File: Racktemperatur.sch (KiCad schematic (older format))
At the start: 16 parts, among them J1 Conn_01x03, J2 Conn_01x03, J3 Barrel_Jack_MountingPin, Q1 IRLZ44N, U1 74HC595, U2 74HC595, U3 DS18B20

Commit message: Version 1.3 as rack mount
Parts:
- added J4: Screw_Terminal_01x02, TerminalBlock:TerminalBlock_bornier-2_P5.08mm, symbol Connector:Screw_Terminal_01x02
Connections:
- net GND: now also J4.1 (Pin_1)
- net at A1.16 (D13): now also J4.2 (Pin_2)
- no-connect marks 22 -> 25
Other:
- moved on the sheet: R1, R2
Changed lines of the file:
@@
 EESchema Schematic File Version 4
 LIBS:Racktemperatur-cache
-EELAYER 29 0
+EELAYER 30 0
 EELAYER END
 $Descr A4 11693 8268
@@
 Sheet 1 1
 Title "Rack Temperature Control"
-Date "2019-06-03"
-Rev "1.2"
+Date "2019-10-25"
+Rev "1.3"
 Comp "haus-automatisierung.com"
 Comment1 "Matthias Kleine"
@@
 U 1 1 5CA724F1
 P 3800 5300
-F 0 "U1" H 3800 6078 50  0000 C CNN
-F 1 "74HC595" H 3800 5987 50  0000 C CNN
+F 0 "U1" H 3550 5850 50  0000 C CNN
+F 1 "74HC595" H 4000 5850 50  0000 C CNN
 F 2 "Package_DIP:DIP-16_W7.62mm_LongPads" H 3800 5300 50  0001 C CNN
 F 3 "http://www.ti.com/lit/ds/symlink/sn74hc595.pdf" H 3800 5300 50  0001 C CNN
@@
 U 1 1 5CA72541
 P 6450 5250
-F 0 "U2" H 6450 6028 50  0000 C CNN
-F 1 "74HC595" H 6450 5937 50  0000 C CNN
+F 0 "U2" H 6200 5800 50  0000 C CNN
+F 1 "74HC595" H 6650 5800 50  0000 C CNN
 F 2 "Package_DIP:DIP-16_W7.62mm_LongPads" H 6450 5250 50  0001 C CNN
 F 3 "http://www.ti.com/lit/ds/symlink/sn74hc595.pdf" H 6450 5250 50  0001 C CNN
@@
 U 1 1 5CA72A4D
 P 5650 3100
-F 0 "A1" H 5650 2014 50  0000 C CNN
-F 1 "Arduino_Nano_v3.x" H 5650 1923 50  0000 C CNN
+F 0 "A1" H 6000 4050 50  0000 C CNN
+F 1 "Arduino_Nano_v3.x" H 5050 4050 50  0000 C CNN
 F 2 "Module:Arduino_Nano_WithMountingHoles" H 5800 2150 50  0001 L CNN
 F 3 "http://www.mouser.com/pdfdocs/Gravitech_Arduino_Nano3_0.pdf" H 5650 2100 50  0001 C CNN
@@
 Connection ~ 5650 6250
 Wire Wire Line
-	5650 4100 5650 5450
+	5650 4100 5650 4250
 Wire Wire Line
 	5750 2100 5750 1950
@@
 L Device:R R1
 U 1 1 5CA7E658
-P 5400 6100
-F 0 "R1" H 5470 6146 50  0000 L CNN
-F 1 "100Ω" H 5470 6055 50  0000 L CNN
-F 2 "Resistor_SMD:R_0805_2012Metric_Pad1.15x1.40mm_HandSolder" V 5330 6100 50  0001 C CNN
-F 3 "~" H 5400 6100 50  0001 C CNN
-	1    5400 6100
+P 5500 6100
+F 0 "R1" H 5570 6146 50  0000 L CNN
+F 1 "100Ω" H 5570 6055 50  0000 L CNN
+F 2 "Resistor_SMD:R_0805_2012Metric_Pad1.15x1.40mm_HandSolder" V 5430 6100 50  0001 C CNN
+F 3 "~" H 5500 6100 50  0001 C CNN
+	1    5500 6100
 	1    0    0    -1
 $EndComp
@@
 L Device:R R2
 U 1 1 5CA7E6C1
-P 8050 6100
-F 0 "R2" H 8120 6146 50  0000 L CNN
-F 1 "100Ω" H 8120 6055 50  0000 L CNN
-F 2 "Resistor_SMD:R_0805_2012Metric_Pad1.15x1.40mm_HandSolder" V 7980 6100 50  0001 C CNN
-F 3 "~" H 8050 6100 50  0001 C CNN
-	1    8050 6100
-	1    0    0    -1
-$EndComp
-Wire Wire Line
-	8050 6250 6450 6250
+P 8100 6100
+F 0 "R2" H 8170 6146 50  0000 L CNN
+F 1 "100Ω" H 8170 6055 50  0000 L CNN
+F 2 "Resistor_SMD:R_0805_2012Metric_Pad1.15x1.40mm_HandSolder" V 8030 6100 50  0001 C CNN
+F 3 "~" H 8100 6100 50  0001 C CNN
+	1    8100 6100
+	1    0    0    -1
+$EndComp
+Wire Wire Line
+	8100 6250 6450 6250
 Connection ~ 6450 6250
 $Comp
@@
 U 1 1 5CA7516E
 P 7500 5250
-F 0 "AFF2" H 7500 5917 50  0000 C CNN
-F 1 "LTS-6980HR" H 7500 5826 50  0000 C CNN
+F 0 "AFF2" H 7200 5800 50  0000 C CNN
+F 1 "LTS-6980HR" H 7650 5800 50  0000 C CNN
 F 2 "Display_7Segment:7SegmentLED_LTS6760_LTS6780" H 7500 4650 50  0001 C CNN
 F 3 "http://datasheet.octopart.com/LTS-6960HR-Lite-On-datasheet-11803242.pdf" H 7500 5250 50  0001 C CNN
@@
 	3250 3500 4950 3500
 Wire Wire Line
-	3800 6250 5400 6250
-Wire Wire Line
-	5350 5000 5400 5000
-Wire Wire Line
-	5400 5000 5400 5950
-Wire Wire Line
-	5400 6250 5650 6250
-Connection ~ 5400 6250
+	3800 6250 5500 6250
+Wire Wire Line
+	5350 5000 5500 5000
+Wire Wire Line
+	5500 5000 5500 5950
+Wire Wire Line
+	5500 6250 5650 6250
+Connection ~ 5500 6250
 Wire Wire Line
 	4200 5800 4350 5800
@@
 	8550 3100 8550 6250
 Wire Wire Line
-	8550 6250 8050 6250
-Connection ~ 8050 6250
-Wire Wire Line
-	8000 4950 8050 4950
-Wire Wire Line
-	8050 4950 8050 5950
+	8550 6250 8100 6250
+Connection ~ 8100 6250
+Wire Wire Line
+	8000 4950 8100 4950
+Wire Wire Line
+	8100 4950 8100 5950
 Wire Wire Line
 	4200 5000 4250 5000
@@
 U 1 1 5CA881EC
 P 4850 5300
-F 0 "AFF1" H 4850 5967 50  0000 C CNN
-F 1 "LTS-6980HR" H 4850 5876 50  0000 C CNN
+F 0 "AFF1" H 4550 5850 50  0000 C CNN
+F 1 "LTS-6980HR" H 5000 5850 50  0000 C CNN
 F 2 "Display_7Segment:7SegmentLED_LTS6760_LTS6780" H 4850 4700 50  0001 C CNN
 F 3 "http://datasheet.octopart.com/LTS-6960HR-Lite-On-datasheet-11803242.pdf" H 4850 5300 50  0001 C CNN
@@
 	4250 5100 4250 6200
 Wire Wire Line
-	4250 6200 5300 6200
-Wire Wire Line
-	5300 6200 5300 5600
-Wire Wire Line
-	5300 5600 5350 5600
+	4250 6200 5350 6200
+Wire Wire Line
+	5350 6200 5350 5600
 Wire Wire Line
 	6850 4950 6900 4950
@@
 Wire Wire Line
 	6900 5050 6900 6200
-Wire Wire Line
-	6900 6200 7950 6200
-Wire Wire Line
-	7950 6200 7950 5550
-Wire Wire Line
-	7950 5550 8000 5550
 Wire Wire Line
 	4200 5200 4300 5200
@@
 NoConn ~ 5150 3100
 NoConn ~ 5150 3300
-NoConn ~ 5150 3800
 NoConn ~ 5750 4100
 NoConn ~ 950  3350
@@
 Wire Wire Line
 	1150 3550 1150 3000
+$Comp
+L Connector:Screw_Terminal_01x02 J4
+U 1 1 5DB3DDF3
+P 4300 4250
+F 0 "J4" H 4218 3925 50  0000 C CNN
+F 1 "Screw_Terminal_01x02" H 4218 4016 50  0000 C CNN
+F 2 "TerminalBlock:TerminalBlock_bornier-2_P5.08mm" H 4300 4250 50  0001 C CNN
+F 3 "~" H 4300 4250 50  0001 C CNN
+	1    4300 4250
+	-1   0    0    1
+$EndComp
+Wire Wire Line
+	5150 3800 4850 3800
+Wire Wire Line
+	4850 3800 4850 4150
+Wire Wire Line
+	4850 4150 4500 4150
+Wire Wire Line
+	4500 4250 5650 4250
+Connection ~ 5650 4250
+Wire Wire Line
+	5650 4250 5650 5450
+NoConn ~ 6850 5750
+Wire Wire Line
+	8000 5550 8000 6200
+Wire Wire Line
+	6900 6200 8000 6200
+NoConn ~ 8000 4850
+NoConn ~ 5350 4900
+NoConn ~ 9000 2700
 $EndSCHEMATC

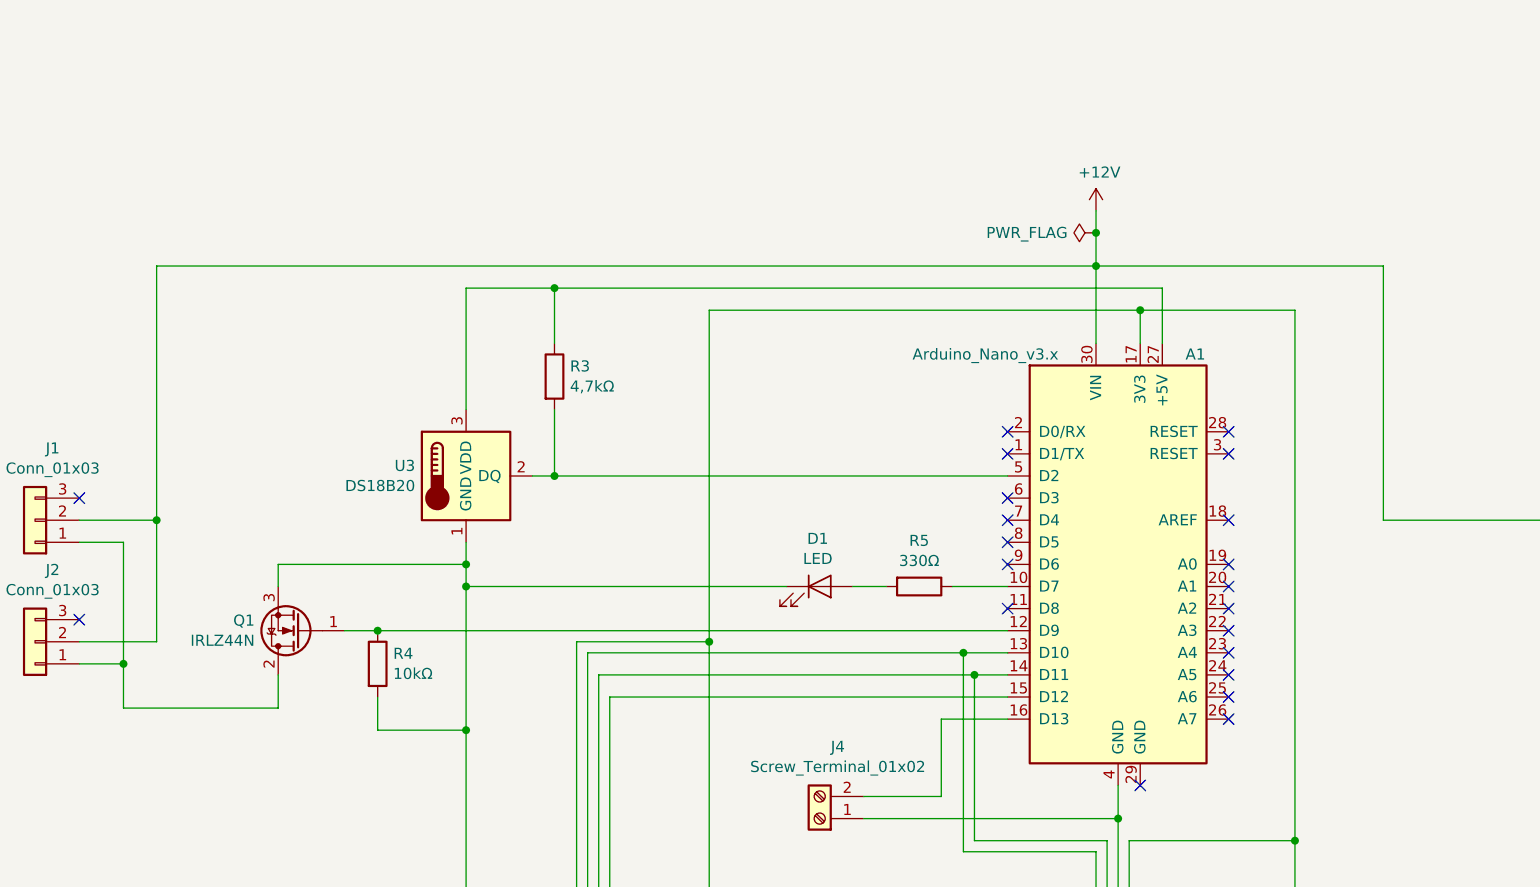
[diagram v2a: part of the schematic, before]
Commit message: Added LM7805
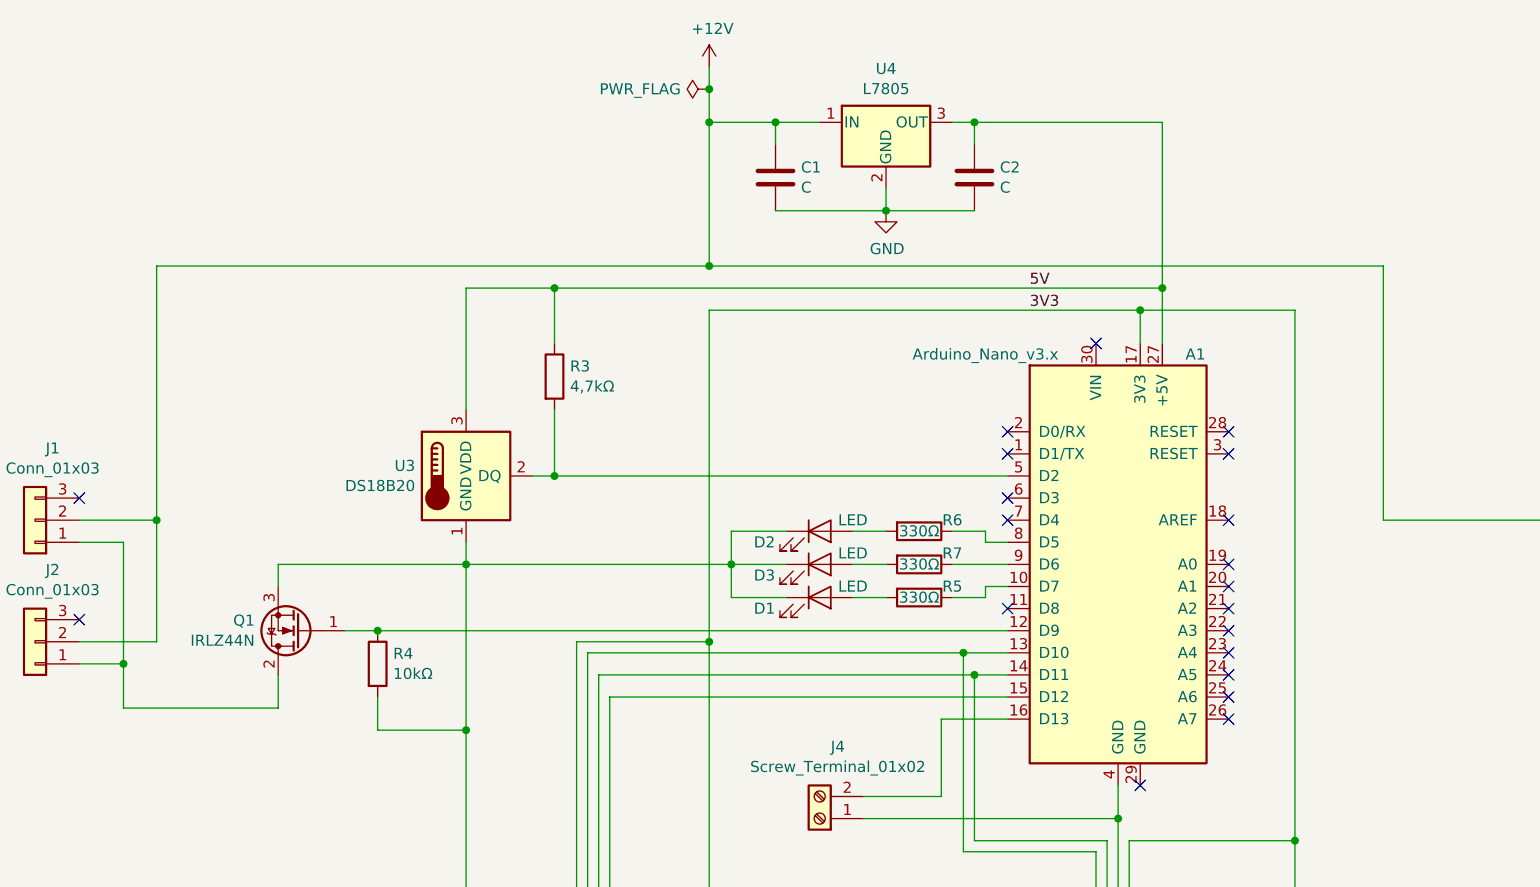
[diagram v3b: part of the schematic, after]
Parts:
- added C1, C2: C, Capacitor_SMD:C_0805_2012Metric_Pad1.15x1.40mm_HandSolder, symbol Device:C
- added D2, D3: LED, LED_SMD:LED_0805_2012Metric_Pad1.15x1.40mm_HandSolder, symbol Device:LED
- added R6, R7: 330Ω, Resistor_SMD:R_0805_2012Metric_Pad1.15x1.40mm_HandSolder, symbol Device:R
- added U4: L7805, Package_TO_SOT_THT:TO-220-3_Horizontal_TabDown, symbol Regulator_Linear:L7805
- D1: footprint LED_THT:LED_D3.0mm -> LED_SMD:LED_0805_2012Metric_Pad1.15x1.40mm_HandSolder
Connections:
- net +12V: now also C1.1, U4.1 (IN); no longer A1.30 (VIN)
- net GND: now also C1.2, C2.2, D2.1 (K), D3.1 (K), U4.2 (GND)
- net 3V3: now reaches A1.17 (3V3), U1.10 (~SRCLR), U1.16 (VCC), U2.10 (~SRCLR), U2.16 (VCC)
- net 5V: now reaches A1.27 (+5V), R3.1, U3.3 (VDD)
- net 5V: now also C2.1, U4.3 (OUT)
- net at A1.8 (D5): now also R6.1
- net at A1.9 (D6): now also R7.1
- new net: D3.2 (A), R7.2
- new net: D2.2 (A), R6.2
- no-connect marks 25 -> 24
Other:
- moved on the sheet: D1, R5
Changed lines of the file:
@@
 Sheet 1 1
 Title "Rack Temperature Control"
-Date "2019-10-25"
-Rev "1.4"
+Date "2019-10-26"
+Rev "1.5"
 Comp "haus-automatisierung.com"
 Comment1 "Matthias Kleine"
@@
 L power:+12V #PWR01
 U 1 1 5CA72BD7
-P 5550 1500
-F 0 "#PWR01" H 5550 1350 50  0001 C CNN
-F 1 "+12V" H 5565 1673 50  0000 C CNN
-F 2 "" H 5550 1500 50  0001 C CNN
-F 3 "" H 5550 1500 50  0001 C CNN
-	1    5550 1500
+P 3800 850
+F 0 "#PWR01" H 3800 700 50  0001 C CNN
+F 1 "+12V" H 3815 1023 50  0000 C CNN
+F 2 "" H 3800 850 50  0001 C CNN
+F 3 "" H 3800 850 50  0001 C CNN
+	1    3800 850
 	1    0    0    -1
 $EndComp
@@
 Connection ~ 5750 1950
 Wire Wire Line
-	5550 1500 5550 1600
+	3800 850  3800 950
 Wire Wire Line
 	3400 5500 3250 5500
@@
 L power:PWR_FLAG #FLG0101
 U 1 1 5CAA3B6E
-P 5550 1600
-F 0 "#FLG0101" H 5550 1675 50  0001 C CNN
-F 1 "PWR_FLAG" V 5550 1728 50  0000 L CNN
-F 2 "" H 5550 1600 50  0001 C CNN
-F 3 "~" H 5550 1600 50  0001 C CNN
-	1    5550 1600
+P 3800 950
+F 0 "#FLG0101" H 3800 1025 50  0001 C CNN
+F 1 "PWR_FLAG" V 3800 1078 50  0000 L CNN
+F 2 "" H 3800 950 50  0001 C CNN
+F 3 "~" H 3800 950 50  0001 C CNN
+	1    3800 950
 	0    -1   -1   0
 $EndComp
@@
 Wire Wire Line
 	3800 3450 3800 4700
-Connection ~ 5550 1600
-Wire Wire Line
-	5550 1600 5550 1750
+Connection ~ 3800 950
+Wire Wire Line
+	3800 950  3800 1100
 Wire Wire Line
 	5150 3400 2300 3400
@@
 	1850 3100 2700 3100
 Connection ~ 2700 3100
-Wire Wire Line
-	2700 3100 2700 3200
 $Comp
 L Connector_Generic:Conn_01x03 J1
@@
 $EndComp
 Wire Wire Line
-	5550 1750 1300 1750
-Connection ~ 5550 1750
-Wire Wire Line
-	5550 1750 5550 2100
-Wire Wire Line
 	1850 3600 1850 3750
 Wire Wire Line
 	1850 3750 1150 3750
-$Comp
-L Device:R R5
-U 1 1 5CAE0B2A
-P 4750 3200
-F 0 "R5" V 4543 3200 50  0000 C CNN
-F 1 "330Ω" V 4634 3200 50  0000 C CNN
-F 2 "Resistor_SMD:R_0805_2012Metric_Pad1.15x1.40mm_HandSolder" V 4680 3200 50  0001 C CNN
-F 3 "~" H 4750 3200 50  0001 C CNN
-	1    4750 3200
-	0    1    1    0
-$EndComp
-$Comp
-L Device:LED D1
-U 1 1 5CAE0E3B
-P 4300 3200
-F 0 "D1" H 4291 3416 50  0000 C CNN
-F 1 "LED" H 4291 3325 50  0000 C CNN
-F 2 "LED_THT:LED_D3.0mm" H 4300 3200 50  0001 C CNN
-F 3 "~" H 4300 3200 50  0001 C CNN
-	1    4300 3200
-	1    0    0    -1
-$EndComp
-Wire Wire Line
-	5150 3200 4900 3200
-Wire Wire Line
-	4600 3200 4450 3200
-Wire Wire Line
-	4150 3200 2700 3200
-Connection ~ 2700 3200
-Wire Wire Line
-	2700 3200 2700 3850
+Wire Wire Line
+	4600 3250 4450 3250
 $Comp
 L Connector:Barrel_Jack_MountingPin J3
@@
 Wire Wire Line
 	6850 2900 6850 1750
-Wire Wire Line
-	6850 1750 5550 1750
 Wire Wire Line
 	8700 3100 8550 3100
@@
 NoConn ~ 5150 2800
 NoConn ~ 5150 2900
-NoConn ~ 5150 3000
-NoConn ~ 5150 3100
 NoConn ~ 5150 3300
 NoConn ~ 5750 4100
@@
 NoConn ~ 5350 4900
 NoConn ~ 9000 2700
+Wire Wire Line
+	4600 3100 4450 3100
+Wire Wire Line
+	5150 3100 4900 3100
+$Comp
+L Device:LED D3
+U 1 1 5DB55BB8
+P 4300 3100
+F 0 "D3" H 4050 3050 50  0000 C CNN
+F 1 "LED" H 4450 3150 50  0000 C CNN
+F 2 "LED_SMD:LED_0805_2012Metric_Pad1.15x1.40mm_HandSolder" H 4300 3100 50  0001 C CNN
+F 3 "~" H 4300 3100 50  0001 C CNN
+	1    4300 3100
+	1    0    0    -1
+$EndComp
+$Comp
+L Device:LED D1
+U 1 1 5CAE0E3B
+P 4300 3250
+F 0 "D1" H 4050 3200 50  0000 C CNN
+F 1 "LED" H 4450 3300 50  0000 C CNN
+F 2 "LED_SMD:LED_0805_2012Metric_Pad1.15x1.40mm_HandSolder" H 4300 3250 50  0001 C CNN
+F 3 "~" H 4300 3250 50  0001 C CNN
+	1    4300 3250
+	1    0    0    -1
+$EndComp
+$Comp
+L Device:R R5
+U 1 1 5CAE0B2A
+P 4750 3250
+F 0 "R5" V 4700 3400 50  0000 C CNN
+F 1 "330Ω" V 4750 3250 50  0000 C CNN
+F 2 "Resistor_SMD:R_0805_2012Metric_Pad1.15x1.40mm_HandSolder" V 4680 3250 50  0001 C CNN
+F 3 "~" H 4750 3250 50  0001 C CNN
+	1    4750 3250
+	0    1    1    0
+$EndComp
+$Comp
+L Device:R R7
+U 1 1 5DB5D3D3
+P 4750 3100
+F 0 "R7" V 4700 3250 50  0000 C CNN
+F 1 "330Ω" V 4750 3100 50  0000 C CNN
+F 2 "Resistor_SMD:R_0805_2012Metric_Pad1.15x1.40mm_HandSolder" V 4680 3100 50  0001 C CNN
+F 3 "~" H 4750 3100 50  0001 C CNN
+	1    4750 3100
+	0    1    1    0
+$EndComp
+$Comp
+L Device:LED D2
+U 1 1 5DB88188
+P 4300 2950
+F 0 "D2" H 4050 2900 50  0000 C CNN
+F 1 "LED" H 4450 3000 50  0000 C CNN
+F 2 "LED_SMD:LED_0805_2012Metric_Pad1.15x1.40mm_HandSolder" H 4300 2950 50  0001 C CNN
+F 3 "~" H 4300 2950 50  0001 C CNN
+	1    4300 2950
+	1    0    0    -1
+$EndComp
+$Comp
+L Device:R R6
+U 1 1 5DB88996
+P 4750 2950
+F 0 "R6" V 4700 3100 50  0000 C CNN
+F 1 "330Ω" V 4750 2950 50  0000 C CNN
+F 2 "Resistor_SMD:R_0805_2012Metric_Pad1.15x1.40mm_HandSolder" V 4680 2950 50  0001 C CNN
+F 3 "~" H 4750 2950 50  0001 C CNN
+	1    4750 2950
+	0    1    1    0
+$EndComp
+Wire Wire Line
+	5150 3200 5050 3200
+Wire Wire Line
+	5050 3200 5050 3250
+Wire Wire Line
+	5050 3250 4900 3250
+Wire Wire Line
+	5150 3000 5050 3000
+Wire Wire Line
+	5050 3000 5050 2950
+Wire Wire Line
+	5050 2950 4900 2950
+Wire Wire Line
+	2700 3100 2700 3850
+Wire Wire Line
+	4600 2950 4450 2950
+Wire Wire Line
+	4150 2950 3900 2950
+Wire Wire Line
+	3900 2950 3900 3100
+Wire Wire Line
+	3900 3100 2700 3100
+Wire Wire Line
+	4150 3250 3900 3250
+Wire Wire Line
+	3900 3250 3900 3100
+Connection ~ 3900 3100
+Wire Wire Line
+	4150 3100 3900 3100
+Text Label 5250 1850 0    50   ~ 0
+5V
+Text Label 5250 1950 0    50   ~ 0
+3V3
+$Comp
+L Regulator_Linear:L7805 U4
+U 1 1 5DC4AC8E
+P 4600 1100
+F 0 "U4" H 4600 1342 50  0000 C CNN
+F 1 "L7805" H 4600 1251 50  0000 C CNN
+F 2 "Package_TO_SOT_THT:TO-220-3_Horizontal_TabDown" H 4625 950 50  0001 L CIN
+F 3 "http://www.st.com/content/ccc/resource/technical/document/datasheet/41/4f/b3/b0/12/d4/47/88/CD00000444.pdf/files/CD00000444.pdf/jcr:content/translations/en.CD00000444.pdf" H 4600 1050 50  0001 C CNN
+	1    4600 1100
+	1    0    0    -1
+$EndComp
+NoConn ~ 5550 2100
+Connection ~ 3800 1750
+Wire Wire Line
+	3800 1750 1300 1750
+Wire Wire Line
+	3800 1750 6850 1750
+Wire Wire Line
+	4900 1100 5000 1100
+Wire Wire Line
+	5850 1100 5850 1850
+Connection ~ 5850 1850
+Wire Wire Line
+	4300 1100 4100 1100
+Connection ~ 3800 1100
+Wire Wire Line
+	3800 1100 3800 1750
+$Comp
+L power:GND #PWR03
+U 1 1 5DC84E03
+P 4600 1500
+F 0 "#PWR03" H 4600 1250 50  0001 C CNN
+F 1 "GND" H 4605 1327 50  0000 C CNN
+F 2 "" H 4600 1500 50  0001 C CNN
+F 3 "" H 4600 1500 50  0001 C CNN
+	1    4600 1500
+	1    0    0    -1
+$EndComp
+Wire Wire Line
+	4600 1500 4600 1400
+$Comp
+L Device:C C1
+U 1 1 5DC8DB2A
+P 4100 1350
+F 0 "C1" H 4215 1396 50  0000 L CNN
+F 1 "C" H 4215 1305 50  0000 L CNN
+F 2 "Capacitor_SMD:C_0805_2012Metric_Pad1.15x1.40mm_HandSolder" H 4138 1200 50  0001 C CNN
+F 3 "~" H 4100 1350 50  0001 C CNN
+	1    4100 1350
+	1    0    0    -1
+$EndComp
+$Comp
+L Device:C C2
+U 1 1 5DC8E2FC
+P 5000 1350
+F 0 "C2" H 5115 1396 50  0000 L CNN
+F 1 "C" H 5115 1305 50  0000 L CNN
+F 2 "Capacitor_SMD:C_0805_2012Metric_Pad1.15x1.40mm_HandSolder" H 5038 1200 50  0001 C CNN
+F 3 "~" H 5000 1350 50  0001 C CNN
+	1    5000 1350
+	1    0    0    -1
+$EndComp
+Wire Wire Line
+	5000 1200 5000 1100
+Connection ~ 5000 1100
+Wire Wire Line
+	5000 1100 5850 1100
+Wire Wire Line
+	4100 1200 4100 1100
+Connection ~ 4100 1100
+Wire Wire Line
+	4100 1100 3800 1100
+Wire Wire Line
+	5000 1500 4600 1500
+Connection ~ 4600 1500
+Wire Wire Line
+	4100 1500 4600 1500
 $EndSCHEMATC
